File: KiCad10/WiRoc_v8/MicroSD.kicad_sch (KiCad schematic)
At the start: 5 parts, among them J3 Micro_SD_Card_Det1

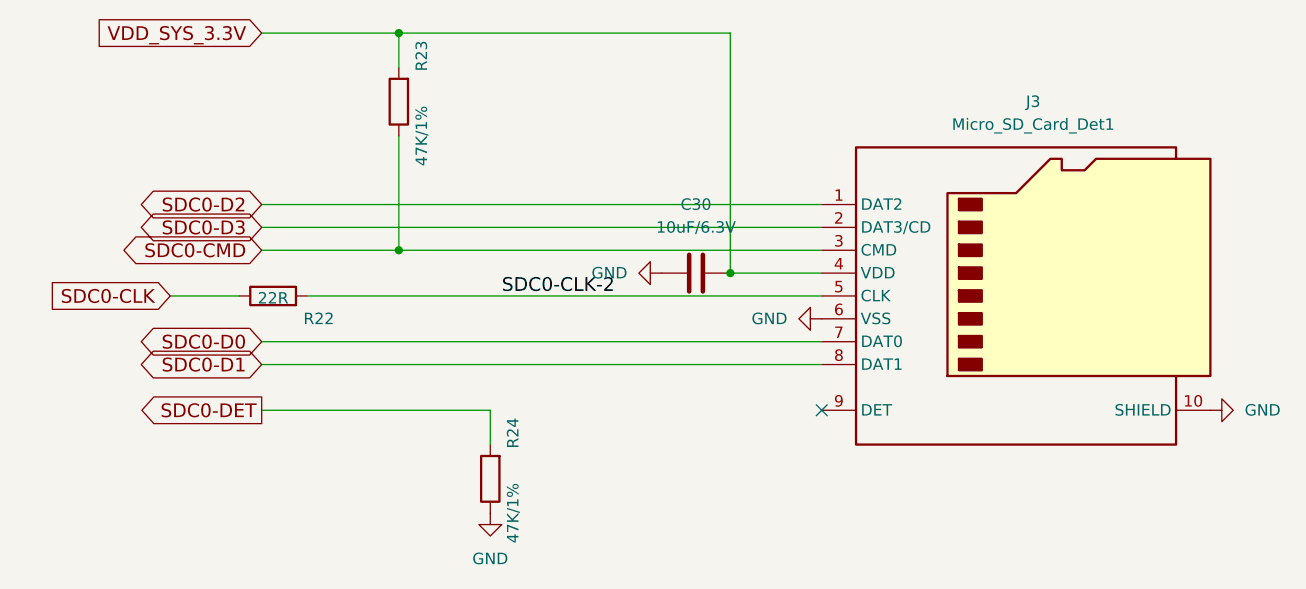
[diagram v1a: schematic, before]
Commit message: add logo, improve layout
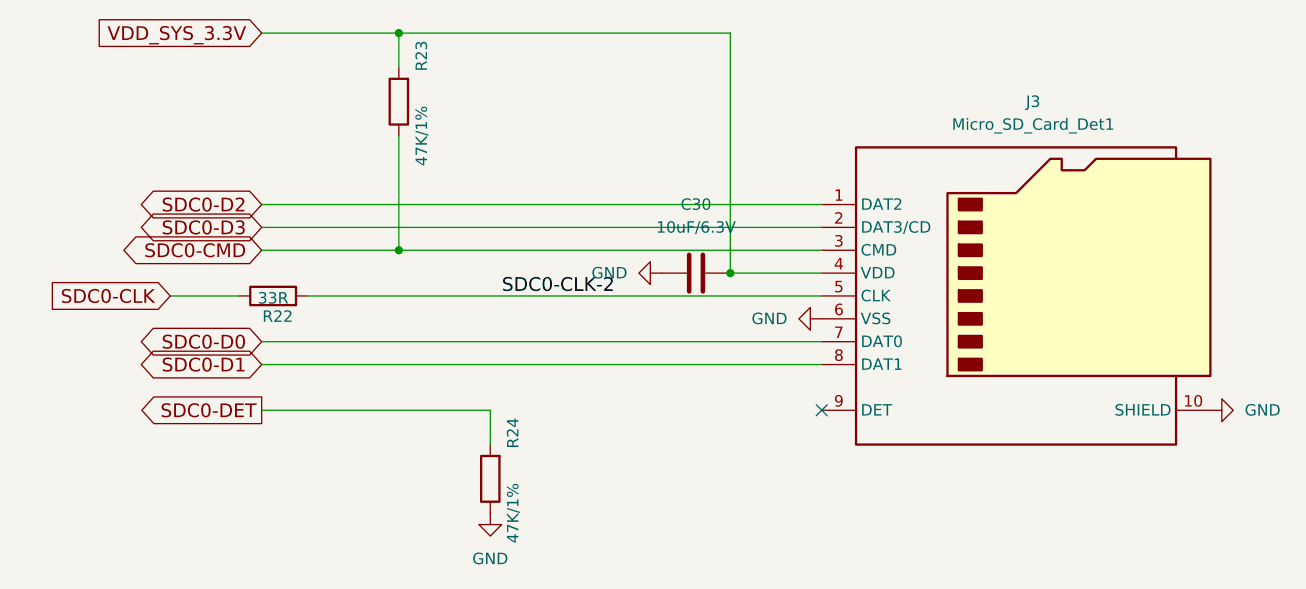
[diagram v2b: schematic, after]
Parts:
- R22: value 22R -> 33R; LCSC Part # C25092 -> C25105; ManufacturerPartNumber 0402WGF220JTCE -> 0402WGF330JTCE
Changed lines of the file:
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@@
 (kicad_sch
-	(version 20260326)
+	(version 20260306)
 	(generator "eeschema")
-	(generator_version "10.99")
+	(generator_version "10.0")
 	(paper "A4")
 	(junction
@@
 		(dnp no)
 		(property "Reference" "R22"
-			(at 69.85 73.66 90)
-			(show_name no)
-			(do_not_autoplace no)
-			(effects
-				(font
-					(size 1.27 1.27)
-				)
-			)
-		)
-		(property "Value" "22R"
+			(at 65.278 73.406 90)
+			(show_name no)
+			(do_not_autoplace no)
+			(effects
+				(font
+					(size 1.27 1.27)
+				)
+			)
+		)
+		(property "Value" "33R"
 			(at 64.77 71.374 90)
 			(show_name no)
@@
 			)
 		)
-		(property "LCSC Part #" "C25092"
+		(property "LCSC Part #" "C25105"
 			(at 64.77 71.12 90)
 			(hide yes)
@@
 			)
 		)
-		(property "ManufacturerPartNumber" "0402WGF220JTCE"
+		(property "ManufacturerPartNumber" "0402WGF330JTCE"
 			(at 64.77 71.12 90)
 			(hide yes)
